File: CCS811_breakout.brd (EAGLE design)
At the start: 52.5 x 43 mm, 48 parts, among them J3 USB-MICROB, U1 ATMEGA328P, U10 CCS811, U11 RFM69HW, U2 TSL2561, U4 MPL115A, U5 FT231XS, U7 SHT31, U8 MCP1703/3.3V, U9 MCP1703CB, Y1 16MHZ

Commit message: Updated brd file
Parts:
- removed C1, C16, C17, C6: 1uF, SparkFun-Capacitors:0805
- removed C11: 0.1uF, SparkFun-Capacitors:0805
- removed C12, C13, C14, C15, C3, C4, C7: 0.1uF, SparkFun-Passives:0805
- removed J2: (no value), SparkFun-Connectors:AVR_ICSP
- removed J3: USB-MICROB, SparkFun-Connectors:USB-MICROB
- removed LED2: (no value), adafruit:CHIPLED_0805
- removed MICS4514: SPARKFUN-SENSORS_MICS-4514, MICS-4514_CO_and_NOx_Sensor_Breakout:SPARKFUN-SENSORS_MICS_10-SMD
- removed MOSFET: SPARKFUN-DISCRETESEMI_MOSFET-NCHANNELBSS138, MICS-4514_CO_and_NOx_Sensor_Breakout:SPARKFUN-DISCRETESEMI_SOT23-3
- removed R10, R9: 47, SparkFun-Passives:0805
- removed R11: SHOTTKY, SparkFun-Passives:0805
- removed R12, R21: 27, SparkFun-Passives:0805
- removed R13: 10K, SparkFun-Passives:0805
- removed R14: 47K, SparkFun-Passives:0805
- removed R15, R18: 82, SparkFun-Passives:0805
- removed R16: 22K, SparkFun-Passives:0805
- removed R17: 51, SparkFun-Passives:0805
- removed R19: 100K, SparkFun-Passives:0805
- removed R20: 100, SparkFun-Passives:0805
- removed R4: 47, SparkFun-Resistors:0805
- removed R5, R6: 10K, SparkFun-Resistors:0805
- removed RX: Green, adafruit:CHIPLED_0805
- removed TX: Red, adafruit:CHIPLED_0805
- removed U1: ATMEGA328P, SparkFun-DigitalIC:TQFP32-08
- removed U11: RFM69HW, RFM69 USB Gateway:LOWPOWERLAB_RFM69W-MINPADS
- removed U2: TSL2561, SparkFun-DigitalIC:FN-6
- removed U4: MPL115A, SparkFun-Sensors:LGA8
- removed U5: FT231XS, SparkFun-DigitalIC:SSOP20_L
- removed U7: SHT31, thomasb9511:SHT3X
- removed U8: MCP1703/3.3V, linear:SOT23
- removed U9: MCP1703CB, linear:SOT23
- removed X1: (no value), adafruit:SMA_EDGELAUNCH
- removed Y1: 16MHZ, SparkFun-FreqCtrl:RESONATOR-SMD
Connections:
- removed net 5V: C17.1, C7.1, MICS4514.F, MICS4514.G, MICS4514.H, MICS4514.J, U9.2
- removed net A0: U1.23
- removed net A7: U1.22
- removed net ANT: U11.ANA, X1.P
- removed net D2: U1.32, U11.DIO0
- removed net D5: U1.9
- removed net DTR: C12.1, J2.10, U5.1
- removed net FTDI_VCC: R10.1, R9.1, U5.13, U5.14, U5.3
- removed net MISO: J2.1, U1.16, U11.MISO
- removed net MOSI: J2.4, U1.15, U11.MOSI
- removed net N$12: C13.1, U4.2
- removed net N$13: MICS4514.C, R15.2
- removed net N$17: RX.C, U5.17
- removed net N$18: TX.C, U5.10
- removed net N$2: R4.1, U1.13
- removed net N$20: MOSFET.3, R17.2, R18.1
- removed net N$23: MOSFET.1, R19.2, R20.1
- removed net N$25: R21.1, U5.12
- removed net N$26: R12.1, U5.11
- removed net N$27: R9.2, RX.A
- removed net N$29: R10.2, TX.A
- removed net N$3: LED2.A, R4.2
- removed net N$32: J3.D-, R21.2
- removed net N$33: J3.D+, R12.2
- removed net N$4: U1.8, Y1.3
- removed net N$5: U1.7, Y1.1
- removed net N$8: MICS4514.A, R18.2
- removed net PRE: R20.2, U1.1
- removed net PWR: C1.1, C16.1, J2.2, R11.1, U8.3, U9.3
- removed net RESET: C12.2, J2.5, R13.1, U1.29
- removed net RX: J2.7, U1.30, U5.20
- removed net SCK: J2.3, U1.17, U11.SCK
- removed net SS: U1.14, U11.NSS
- removed net TX: J2.8, U1.31, U5.4
- removed net VBUS: C11.1, J3.VBUS, R11.2, U5.15
- removed net VNOX: MICS4514.B, R16.2, U1.24
- removed net VRED: MICS4514.D, R14.2, U1.25
- net GND: no longer C1.2, C11.2, C13.2, C14.2, C15.2, C16.2, C17.2, C3.2, C4.2, C6.2, C7.2, J2.6, J3.GND, J3.MT1, J3.MT2, LED2.C, MOSFET.2, R14.1, R15.1, R16.1, R17.1, R19.1, U1.21, U1.3, U1.5, U11.GND, U2.3, U4.3, U5.16, U5.6, U7.P$2, U7.P$7, U7.P$8, U7.PAD, U8.1, U9.1, X1.GND@1, X1.GND@2, X1.GND@3, X1.GND@4, Y1.2
- net SCL: no longer R6.1, U1.28, U2.4, U4.8, U7.P$4
- net SDA: no longer R5.1, U1.27, U2.6, U4.7, U7.P$1
- net VCC: no longer C14.1, C15.1, C3.1, C4.1, C6.1, R13.2, R5.2, R6.2, U1.18, U1.4, U1.6, U11.VDD, U2.1, U4.1, U4.4, U7.P$5, U8.2
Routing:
- net VCC: track 140.0 -> 68.3 mm, vias 5 -> 4
- net SCK: track 59.7 -> 0.00 mm, vias 1 -> 0
- net RX: track 58.0 -> 0.00 mm, vias 3 -> 0
- net DTR: track 57.1 -> 0.00 mm, vias 2 -> 0
- net TX: track 52.0 -> 0.00 mm, vias 5 -> 0
- net RESET: track 51.1 -> 0.00 mm, vias 1 -> 0
- net MISO: track 49.1 -> 0.00 mm, vias 2 -> 0
- net MOSI: track 45.0 -> 0.00 mm, vias 2 -> 0
- net GND: track 55.7 -> 11.1 mm, vias 34 -> 28
- net 5V: track 42.6 -> 0.00 mm, vias 2 -> 0
- net PWR: track 35.1 -> 0.00 mm
- net VRED: track 33.0 -> 0.00 mm, vias 2 -> 0
- net VNOX: track 30.9 -> 0.00 mm
- net D2: track 29.8 -> 0.00 mm, vias 3 -> 0
- net N$2: track 28.6 -> 0.00 mm, vias 2 -> 0
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
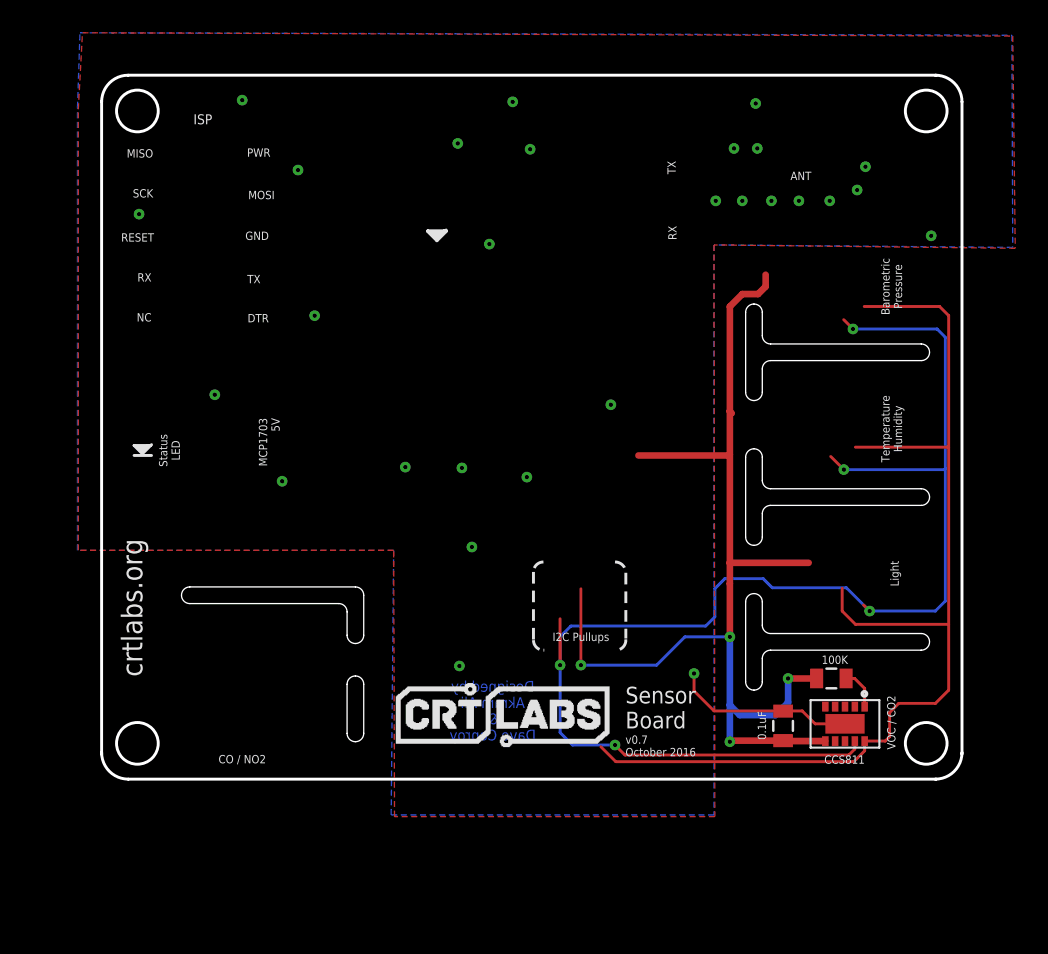
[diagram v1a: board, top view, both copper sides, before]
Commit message: Added 1x4 header
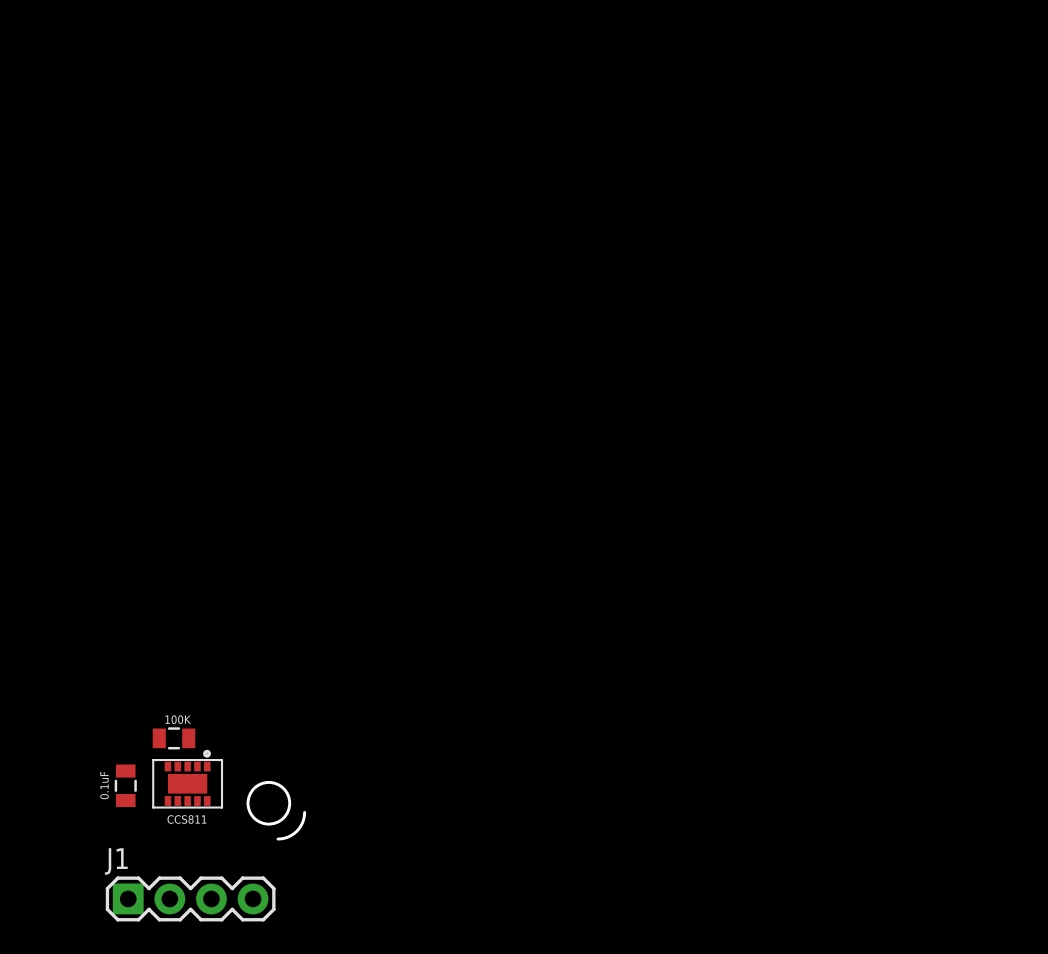
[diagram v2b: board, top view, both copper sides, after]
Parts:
- added J1: (no value), SparkFun-Connectors:1X04
- moved C5 40.3 mm to (4.88, 5.54)
- moved R2 40.3 mm to (7.82, 8.43)
- moved U10 40.3 mm to (6.65, 7.01)
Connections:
- net GND: now also J1.1
- net SCL: now also J1.3
- net SDA: now also J1.4
- net VCC: now also J1.2
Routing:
- net SDA: track 85.6 -> 0.00 mm, vias 5 -> 0
- net VCC: track 68.3 -> 0.00 mm, vias 4 -> 0
- net SCL: track 66.8 -> 0.00 mm
- net GND: track 11.1 -> 0.00 mm, vias 28 -> 0
- net N$1: track 2.50 -> 0.00 mm
- removed copper zone on layer 1, net GND
- removed copper zone on layer 16, net GND
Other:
- board size 52.5 x 43 mm -> 3.5 x 3.5 mm
- board text removed: "ANT"
- board text removed: "Barometric Pressure"
- board text removed: "CO / NO2"
- board text removed: "DTR"
- board text removed: "Designed by Akram Ali & Dave Conroy"
- board text removed: "GND"
- board text removed: "I2C Pullups"
- board text removed: "ISP"
- board text removed: "Light"
- board text removed: "MCP1703 5V"
- board text removed: "MISO"
- board text removed: "MOSI"
- board text removed: "NC"
- board text removed: "PWR"
- board text removed: "RESET"
- board text removed: "RX"
- board text removed: "SCK"
- board text removed: "Sensor Board"
- board text removed: "Status LED"
- board text removed: "TX"
- board text removed: "Temperature Humidity"
- board text removed: "VOC / CO2"
- board text removed: "crtlabs.org"
- board text removed: "v0.7 October 2016"

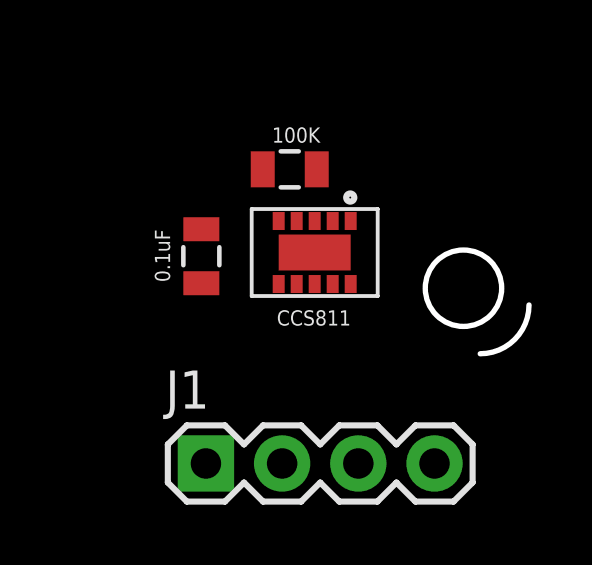
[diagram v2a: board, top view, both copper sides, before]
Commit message: Updated the board layout
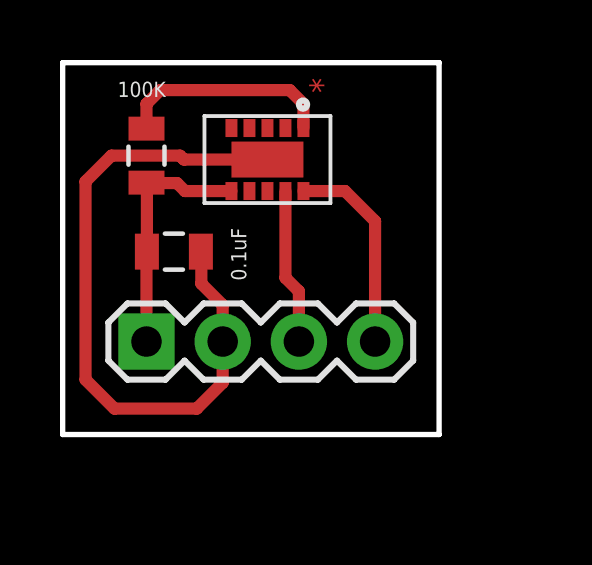
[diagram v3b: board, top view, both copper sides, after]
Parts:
- moved R2 4.80 mm to (3.05, 8.89), turned to 270 degrees
- moved J1 4.52 mm to (3.05, 2.69)
- moved U10 3.48 mm to (5.08, 10.1)
- moved C5 0.93 mm to (3.96, 5.69), turned to 0 degrees
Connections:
- net GND: now also J1.2; no longer J1.1
- net SCL: now also J1.4; no longer J1.3
- net SDA: now also J1.3; no longer J1.4
- net VCC: now also J1.1; no longer J1.2
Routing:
- net GND: track 0.00 -> 23.1 mm
- net VCC: track 0.00 -> 8.24 mm
- net N$1: track 0.00 -> 7.25 mm
- net SCL: track 0.00 -> 6.82 mm
- net SDA: track 0.00 -> 5.20 mm
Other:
- board size 3.5 x 3.5 mm -> 12.5 x 12.4 mm
- board text added: "*"
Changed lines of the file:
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@@
 <board>
 <plain>
-<circle x="13.6144" y="4.4704" radius="1.27304375" width="0.1778" layer="20"/>
-<wire x1="14.1732" y1="2.286" x2="15.7988" y2="3.9116" width="0.1778" layer="20" curve="90"/>
+<wire x1="0.254" y1="-0.4064" x2="12.8016" y2="-0.4064" width="0.1778" layer="20"/>
+<wire x1="12.8016" y1="-0.4064" x2="12.8016" y2="11.9888" width="0.1778" layer="20"/>
+<wire x1="12.8016" y1="11.9888" x2="0.254" y2="11.9888" width="0.1778" layer="20"/>
+<wire x1="0.254" y1="11.9888" x2="0.254" y2="-0.4064" width="0.1778" layer="20"/>
+<text x="8.4836" y="11.4808" size="0.8128" layer="1" font="vector" ratio="12" rot="R270">*</text>
 </plain>
 <attributes>
@@
 </autorouter>
 <elements>
-<element name="U10" library="CCS811" package="LGA" value="CCS811" x="6.6548" y="7.0104" smashed="yes" rot="R270">
-<attribute name="VALUE" x="7.3914" y="3.2258" size="0.508" layer="121" font="vector"/>
+<element name="U10" library="CCS811" package="LGA" value="CCS811" x="5.08" y="10.1092" smashed="yes" rot="R270"/>
+<element name="C5" library="SparkFun-Passives" package="0805" value="0.1uF" x="3.9624" y="5.6896" smashed="yes">
+<attribute name="OC_NEWARK" value="unknown" x="3.9624" y="5.6896" size="1.778" layer="27" display="off"/>
+<attribute name="MPN" value="" x="3.9624" y="5.6896" size="1.778" layer="27" display="off"/>
+<attribute name="MF" value="" x="3.9624" y="5.6896" size="1.778" layer="27" display="off"/>
+<attribute name="VALUE" x="6.3754" y="4.7244" size="0.508" layer="121" font="vector" rot="R90"/>
 </element>
-<element name="C5" library="SparkFun-Passives" package="0805" value="0.1uF" x="4.8768" y="5.5372" smashed="yes" rot="R90">
-<attribute name="OC_NEWARK" value="unknown" x="4.8768" y="5.5372" size="1.778" layer="27" rot="R90" display="off"/>
-<attribute name="MPN" value="" x="4.8768" y="5.5372" size="1.778" layer="27" rot="R90" display="off"/>
-<attribute name="MF" value="" x="4.8768" y="5.5372" size="1.778" layer="27" rot="R90" display="off"/>
-<attribute name="VALUE" x="3.8354" y="4.6736" size="0.508" layer="121" font="vector" rot="R90"/>
+<element name="R2" library="SparkFun-Passives" package="0805" value="100K" x="3.048" y="8.89" smashed="yes" rot="R270">
+<attribute name="OC_NEWARK" value="unknown" x="3.048" y="8.89" size="1.778" layer="27" rot="R270" display="off"/>
+<attribute name="MPN" value="" x="3.048" y="8.89" size="1.778" layer="27" rot="R270" display="off"/>
+<attribute name="MF" value="" x="3.048" y="8.89" size="1.778" layer="27" rot="R270" display="off"/>
+<attribute name="VALUE" x="2.0828" y="10.8458" size="0.508" layer="121" font="vector"/>
 </element>
-<element name="R2" library="SparkFun-Passives" package="0805" value="100K" x="7.8232" y="8.4328" smashed="yes" rot="R180">
-<attribute name="OC_NEWARK" value="unknown" x="7.8232" y="8.4328" size="1.778" layer="27" rot="R180" display="off"/>
-<attribute name="MPN" value="" x="7.8232" y="8.4328" size="1.778" layer="27" rot="R180" display="off"/>
-<attribute name="MF" value="" x="7.8232" y="8.4328" size="1.778" layer="27" rot="R180" display="off"/>
-<attribute name="VALUE" x="8.8392" y="9.8298" size="0.508" layer="121" font="vector" rot="R180"/>
-</element>
-<element name="J1" library="SparkFun-Connectors" package="1X04" value="" x="5.0292" y="-1.3716">
-<attribute name="PROD_ID" value="CONN-09696" x="5.0292" y="-1.3716" size="1.778" layer="27" display="off"/>
+<element name="J1" library="SparkFun-Connectors" package="1X04" value="" x="3.048" y="2.6924" smashed="yes">
+<attribute name="PROD_ID" value="CONN-09696" x="3.048" y="2.6924" size="1.778" layer="27" display="off"/>
+<attribute name="VALUE" x="1.778" y="-0.4826" size="1.27" layer="27"/>
 </element>
 </elements>
@@
 <contactref element="U10" pad="11"/>
 <contactref element="C5" pad="2"/>
-<contactref element="J1" pad="1"/>
-<wire x1="4.8768" y1="6.4372" x2="8.6548" y2="5.6604" width="0" layer="19" extent="1-1"/>
-<wire x1="5.0292" y1="-1.3716" x2="4.8768" y2="6.4372" width="0" layer="19" extent="1-1"/>
+<contactref element="J1" pad="2"/>
+<wire x1="5.588" y1="2.6924" x2="5.588" y2="3.9116" width="0.4064" layer="1"/>
+<wire x1="5.588" y1="3.9116" x2="4.8768" y2="4.6228" width="0.4064" layer="1"/>
+<wire x1="4.8768" y1="4.6228" x2="4.8768" y2="5.6752" width="0.4064" layer="1"/>
+<wire x1="4.8768" y1="5.6752" x2="4.8624" y2="5.6896" width="0.4064" layer="1"/>
+<wire x1="7.08" y1="8.7592" x2="4.2964" y2="8.7592" width="0.4064" layer="1"/>
+<wire x1="4.2964" y1="8.7592" x2="4.1656" y2="8.89" width="0.4064" layer="1"/>
+<wire x1="4.1656" y1="8.89" x2="1.8796" y2="8.89" width="0.4064" layer="1"/>
+<wire x1="1.8796" y1="8.89" x2="1.016" y2="8.0264" width="0.4064" layer="1"/>
+<wire x1="1.016" y1="8.0264" x2="1.016" y2="1.4224" width="0.4064" layer="1"/>
+<wire x1="1.016" y1="1.4224" x2="1.9812" y2="0.4572" width="0.4064" layer="1"/>
+<wire x1="1.9812" y1="0.4572" x2="4.7244" y2="0.4572" width="0.4064" layer="1"/>
+<wire x1="4.7244" y1="0.4572" x2="5.588" y2="1.3208" width="0.4064" layer="1"/>
+<wire x1="5.588" y1="1.3208" x2="5.588" y2="2.6924" width="0.4064" layer="1"/>
 </signal>
 <signal name="VCC">
@@
 <contactref element="C5" pad="1"/>
 <contactref element="R2" pad="2"/>
-<contactref element="J1" pad="2"/>
-<wire x1="7.4548" y1="4.6104" x2="6.9232" y2="8.4328" width="0" layer="19" extent="1-1"/>
-<wire x1="4.8768" y1="4.6372" x2="7.4548" y2="4.6104" width="0" layer="19" extent="1-1"/>
-<wire x1="7.5692" y1="-1.3716" x2="7.4548" y2="4.6104" width="0" layer="19" extent="1-1"/>
+<contactref element="J1" pad="1"/>
+<wire x1="3.048" y1="2.6924" x2="3.048" y2="5.6752" width="0.4064" layer="1"/>
+<wire x1="3.048" y1="5.6752" x2="3.0624" y2="5.6896" width="0.4064" layer="1"/>
+<wire x1="3.0624" y1="5.6896" x2="3.0624" y2="7.9756" width="0.4064" layer="1"/>
+<wire x1="5.88" y1="7.7092" x2="4.3304" y2="7.7092" width="0.4064" layer="1"/>
+<wire x1="4.3304" y1="7.7092" x2="4.064" y2="7.9756" width="0.4064" layer="1"/>
+<wire x1="4.064" y1="7.9756" x2="3.0624" y2="7.9756" width="0.4064" layer="1"/>
+<wire x1="3.0624" y1="7.9756" x2="3.048" y2="7.99" width="0.4064" layer="1"/>
 </signal>
 <signal name="SCL">
 <contactref element="U10" pad="10"/>
-<contactref element="J1" pad="3"/>
-<wire x1="10.1092" y1="-1.3716" x2="9.8548" y2="4.6104" width="0" layer="19" extent="1-1"/>
+<contactref element="J1" pad="4"/>
+<wire x1="8.28" y1="7.7092" x2="9.6644" y2="7.7092" width="0.4064" layer="1"/>
+<wire x1="9.6644" y1="7.7092" x2="10.668" y2="6.7056" width="0.4064" layer="1"/>
+<wire x1="10.668" y1="6.7056" x2="10.668" y2="2.6924" width="0.4064" layer="1"/>
 </signal>
 <signal name="SDA">
 <contactref element="U10" pad="9"/>
-<contactref element="J1" pad="4"/>
-<wire x1="12.6492" y1="-1.3716" x2="9.2548" y2="4.6104" width="0" layer="19" extent="1-1"/>
+<contactref element="J1" pad="3"/>
+<wire x1="7.68" y1="7.7092" x2="7.68" y2="4.8168" width="0.4064" layer="1"/>
+<wire x1="7.68" y1="4.8168" x2="8.128" y2="4.3688" width="0.4064" layer="1"/>
+<wire x1="8.128" y1="4.3688" x2="8.128" y2="2.6924" width="0.4064" layer="1"/>
 </signal>
 <signal name="N$1">
 <contactref element="U10" pad="1"/>
 <contactref element="R2" pad="1"/>
-<wire x1="8.7232" y1="8.4328" x2="9.8548" y2="6.7104" width="0" layer="19" extent="1-1"/>
+<wire x1="3.048" y1="9.79" x2="3.048" y2="10.6172" width="0.4064" layer="1"/>
+<wire x1="3.048" y1="10.6172" x2="3.5052" y2="11.0744" width="0.4064" layer="1"/>
+<wire x1="8.28" y1="9.8092" x2="8.28" y2="10.6176" width="0.4064" layer="1"/>
+<wire x1="8.28" y1="10.6176" x2="7.8232" y2="11.0744" width="0.4064" layer="1"/>
+<wire x1="7.8232" y1="11.0744" x2="3.5052" y2="11.0744" width="0.4064" layer="1"/>
 </signal>
 </signals>
